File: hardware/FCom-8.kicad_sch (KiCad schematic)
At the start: 20 parts, among them SW101 SW_DIP_x08, SW102 SW_DIP_x08, SW103 SW_Push, SW104 SW_DIP_x04, U101 65C02, U102 AS6C1008-55PCN, U103 65C22, U104 74HC245, U105 74HC245, U106 74HC04, U107 74LS08, U108 74LS08, U109 74LS21, U110 MCP23S17_SP

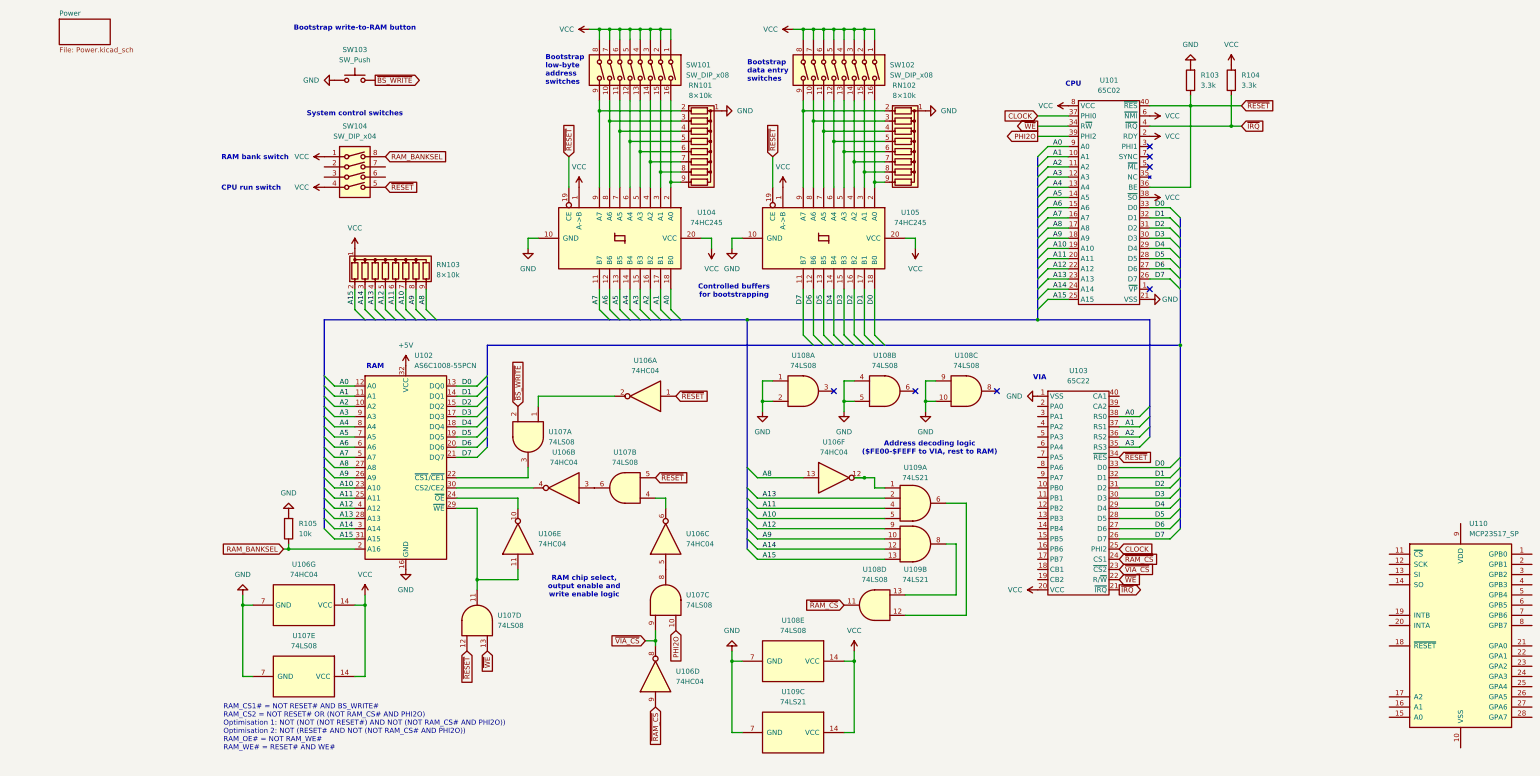
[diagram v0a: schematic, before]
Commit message: Complete schematics and component placements on board
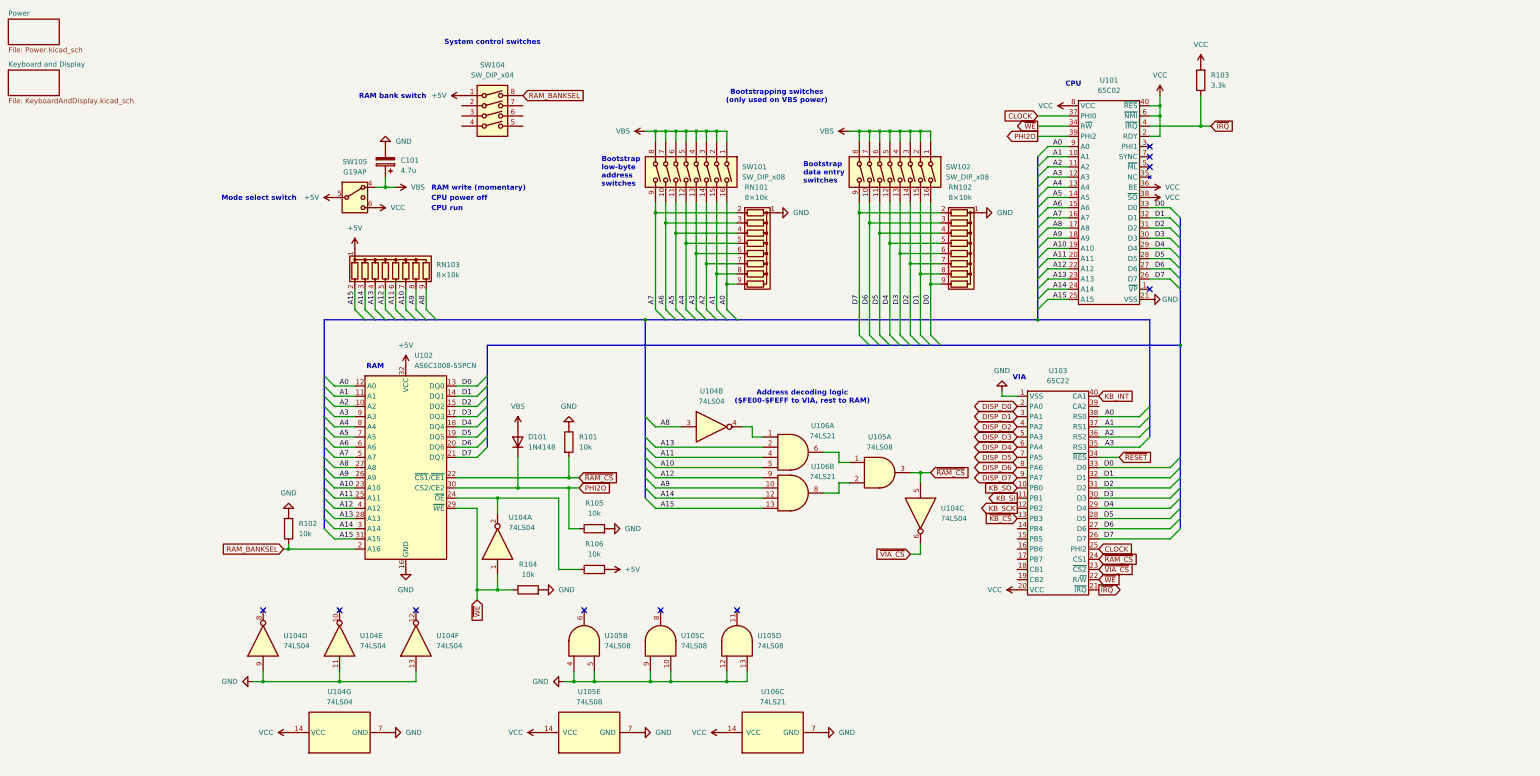
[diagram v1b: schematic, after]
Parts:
- removed R103: 3.3k, Resistor_THT:R_Box_L8.4mm_W2.5mm_P5.08mm, symbol Device:R
- removed SW103: SW_Push, symbol Switch:SW_Push
- removed U104, U105: 74HC245, Package_DIP:DIP-20_W7.62mm, symbol 74xx:74HC245
- removed U106: 74HC04, Package_DIP:DIP-14_W7.62mm, symbol 74xx:74HC04
- removed U107, U108: 74LS08, Package_DIP:DIP-14_W7.62mm, symbol 74xx:74LS08
- removed U109: 74LS21, Package_DIP:DIP-12_W7.62mm, symbol 74xx:74LS21
- removed U110: MCP23S17_SP, Package_DIP:DIP-28_W7.62mm, symbol Interface_Expansion:MCP23S17_SP
- added C101: 4.7u, Capacitor_THT:CP_Radial_D5.0mm_P2.00mm, symbol Device:C_Polarized
- added D101: 1N4148, Diode_THT:D_DO-35_SOD27_P7.62mm_Horizontal, symbol Diode:1N4148
- added R101, R104, R105, R106: 10k, Resistor_THT:R_Axial_DIN0207_L6.3mm_D2.5mm_P7.62mm_Horizontal, symbol Device:R
- added SW105: G19AP, Connector_PinHeader_2.54mm:PinHeader_1x03_P2.54mm_Vertical, symbol Switch:SW_SPDT_MSM
- added U104: 74LS04, Package_DIP:DIP-14_W7.62mm, symbol 74xx:74LS04
- added U105: 74LS08, Package_DIP:DIP-14_W7.62mm, symbol 74xx:74LS08
- added U106: 74LS21, Package_DIP:DIP-14_W7.62mm, symbol 74xx:74LS21
- R102: renamed from R105; footprint Resistor_THT:R_Box_L8.4mm_W2.5mm_P5.08mm -> Resistor_THT:R_Axial_DIN0207_L6.3mm_D2.5mm_P7.62mm_Horizontal
- R103: renamed from R104; footprint Resistor_THT:R_Box_L8.4mm_W2.5mm_P5.08mm -> Resistor_THT:R_Axial_DIN0207_L6.3mm_D2.5mm_P7.62mm_Horizontal
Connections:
- net +5V: now also RN103.1 (common), SW104.1, R106.2, SW105.5
- net A0: now also RN101.9 (R8), SW101.16
- net A1: now also RN101.8 (R7), SW101.15
- net A10: now also U106.5
- net A11: now also U106.4
- net A12: now also U106.9
- net A13: now also U106.2
- net A14: now also U106.12
- net A15: now also U106.13
- net A2: now also RN101.7 (R6), SW101.14
- net A3: now also RN101.6 (R5), SW101.13
- net A4: now also RN101.5 (R4), SW101.12
- net A5: now also RN101.4 (R3), SW101.11
- net A6: now also RN101.3 (R2), SW101.10
- net A7: now also RN101.2 (R1), SW101.9
- net A8: now also U104.3
- net A9: now also U106.10
- net D0: now also RN102.9 (R8), SW102.16
- net D1: now also RN102.8 (R7), SW102.15
- net D2: now also RN102.7 (R6), SW102.14
- net D3: now also RN102.6 (R5), SW102.13
- net D4: now also RN102.5 (R4), SW102.12
- net D5: now also RN102.4 (R3), SW102.11
- net D6: now also RN102.3 (R2), SW102.10
- net D7: now also RN102.2 (R1), SW102.9
- net GND: now also C101.2, R101.1, R104.2, R105.2, U104.11, U104.13, U104.7 (GND), U104.9, U105.10, U105.12, U105.13, U105.4, U105.5, U105.7 (GND), U105.9, U106.7 (GND)
- net PHI2O: now also U102.30 (CS2/CE2), D101.1 (K), R105.1
- net VCC: now also U101.36 (BE), U101.40 (~{RES}), SW105.6, U104.14 (VCC), U105.14 (VCC), U106.14 (VCC); no longer RN103.1 (common), SW101.1, SW101.2, SW101.3, SW101.4, SW101.5, SW101.6, SW101.7, SW101.8, SW102.1, SW102.2, SW102.3, SW102.4, SW102.5, SW102.6, SW102.7, SW102.8, SW104.1, SW104.4
- net ~{RAM_CS}: now also U102.22 (~{CS1}/~{CE1}), R101.2, U104.5, U105.3
- net ~{RESET}: no longer SW104.5, U101.36 (BE), U101.40 (~{RES})
- net ~{VIA_CS}: now also U104.6
- net ~{WE}: now also U102.29 (~{WE}), R104.1, U104.1
- net at U102.24 (~{OE}): now also R106.1, U104.2
- net KB_SO: now reaches U103.10 (PB0)
- net KB_SI: now reaches U103.11 (PB1)
- net KB_SCK: now reaches U103.12 (PB2)
- net ~{KB_CS}: now reaches U103.13 (PB3)
- net DISP_D0: now reaches U103.2 (PA0)
- net DISP_D1: now reaches U103.3 (PA1)
- net DISP_D2: now reaches U103.4 (PA2)
- net KB_INT: now reaches U103.40 (CA1)
- net DISP_D3: now reaches U103.5 (PA3)
- net DISP_D4: now reaches U103.6 (PA4)
- net DISP_D5: now reaches U103.7 (PA5)
- net DISP_D6: now reaches U103.8 (PA6)
- net DISP_D7: now reaches U103.9 (PA7)
- new net: U104.4, U106.1
- new net: U105.1, U106.6
- new net: U105.2, U106.8
- new net VBS: C101.1, D101.2 (A), SW101.1, SW101.2, SW101.3, SW101.4, SW101.5, SW101.6, SW101.7, SW101.8, SW102.1, SW102.2, SW102.3, SW102.4, SW102.5, SW102.6, SW102.7, SW102.8, SW105.4
- no-connect marks 7 -> 10
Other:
- added sheet Keyboard and Display (KeyboardAndDisplay.kicad_sch)
- note added: "Bootstrapping switches (only used on VBS power)"
- note added: "CPU power off"
- note added: "CPU run"
- note added: "Mode select switch"
- note added: "RAM write (momentary)"
- note removed: "Bootstrap write-to-RAM button"
- note removed: "CPU run switch"
- note removed: "Controlled buffers for bootstrapping"
- note removed: "RAM chip select, output enable and write enable logic"
- note removed: "RAM_CS1# = NOT RESET# AND BS_WRITE# RAM_CS2 = NOT RESET# OR (NOT RAM_CS# AND PHI2O) Optimisation 1: NOT (NOT (NOT RESET#) AND NOT (NOT RAM_CS# AND PHI2O)) Optimisation 2: NOT (RESET# AND NOT (NOT RAM_CS# AND PHI2O)) RAM_OE# = NOT RAM_WE# RAM_WE# = RESET# AND WE#"
- moved on the sheet: R103, RN101, RN102, SW101, SW102, SW104, U103
